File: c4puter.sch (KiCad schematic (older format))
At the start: 19 parts, among them J7 19V 3A, Q1 AOD4189, Q2 AOD4189, SW1 POWER, SW2 SW

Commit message: TODO: learn to write good commit messages
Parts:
- added C122: 100n, IPC7351-Nominal:CAPC1005X55, symbol C-0402
- added DS19: ACT, smd-semi:LED-0603, symbol LED-0603
- added DS20: POWER, smd-semi:LED-0603, symbol LED-0603
- added J9: PANEL, conn-100mil:CONN-100MIL-M-2x3, symbol CONN-100MIL-M-2x3
- added R14: 51, IPC7351-Nominal:RESC1005X40, symbol R-0402
- added R22, R52: 5k1, IPC7351-Nominal:RESC1005X40, symbol R-0402
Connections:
- net GND: now also C122.2, J9.1, J9.3, J9.5, R22.2, R52.2
- net at R71.2, R73.2, SW1.3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: now also J9.6
- net EC/BTN_PWR: now reaches C57.1, R73.1
- net EC/BTN_AUX: now reaches C59.1, R74.1
- new net: C122.1, R14.2
- new net: DS20.1 (K), R52.1
- new net: DS19.1 (K), R22.1
- new net CPU0/CCLK: R14.1
- new net EC/LED_ACT: DS19.2 (A), J9.4
- new net EC/LED_PWR: DS20.2 (A), J9.2
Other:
- note added: "Layout: route FPGA configuration data with\nstandard multidrop bus layout, rough length\nmatching between data and CCLK, fly-by\ntermination of CCLK."
- moved on the sheet: C57, C59, R73, R74

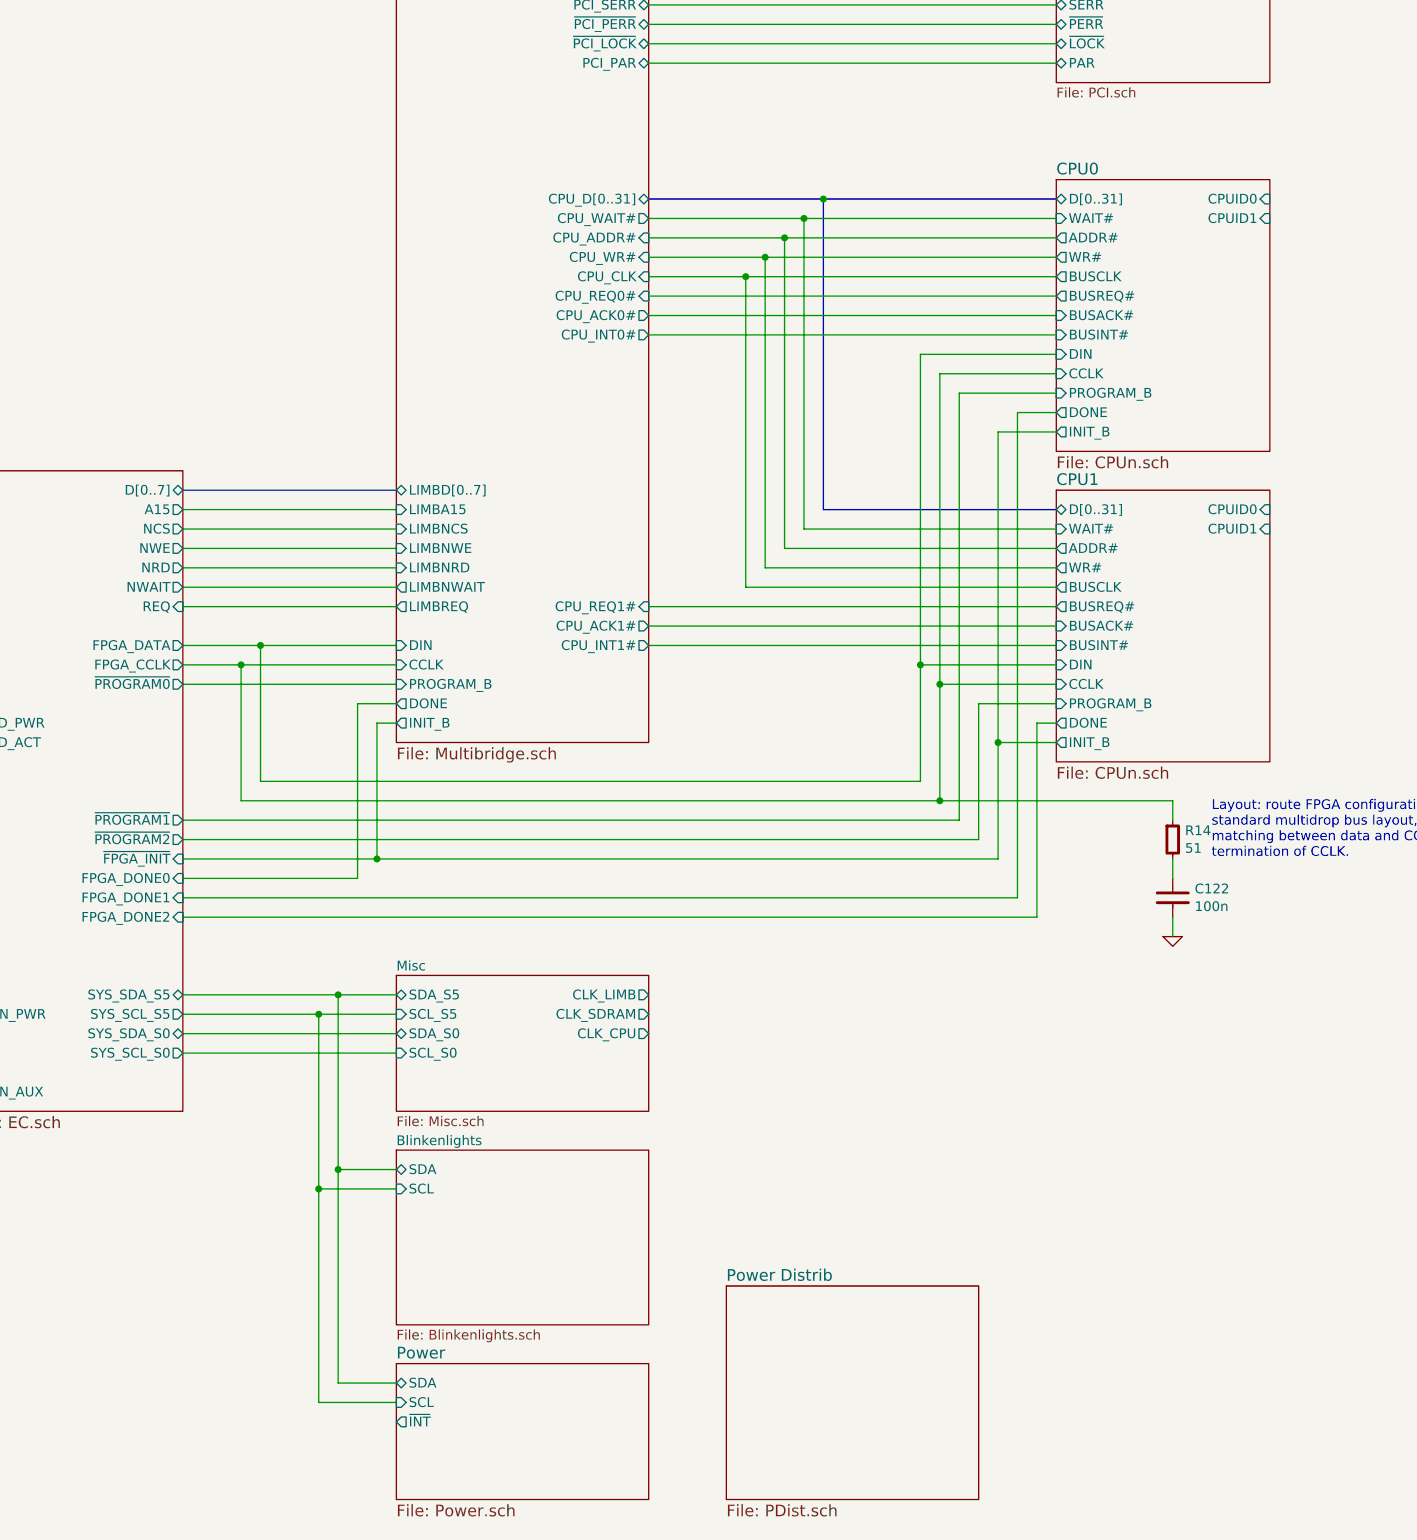
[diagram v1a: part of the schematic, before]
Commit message: Route clocks
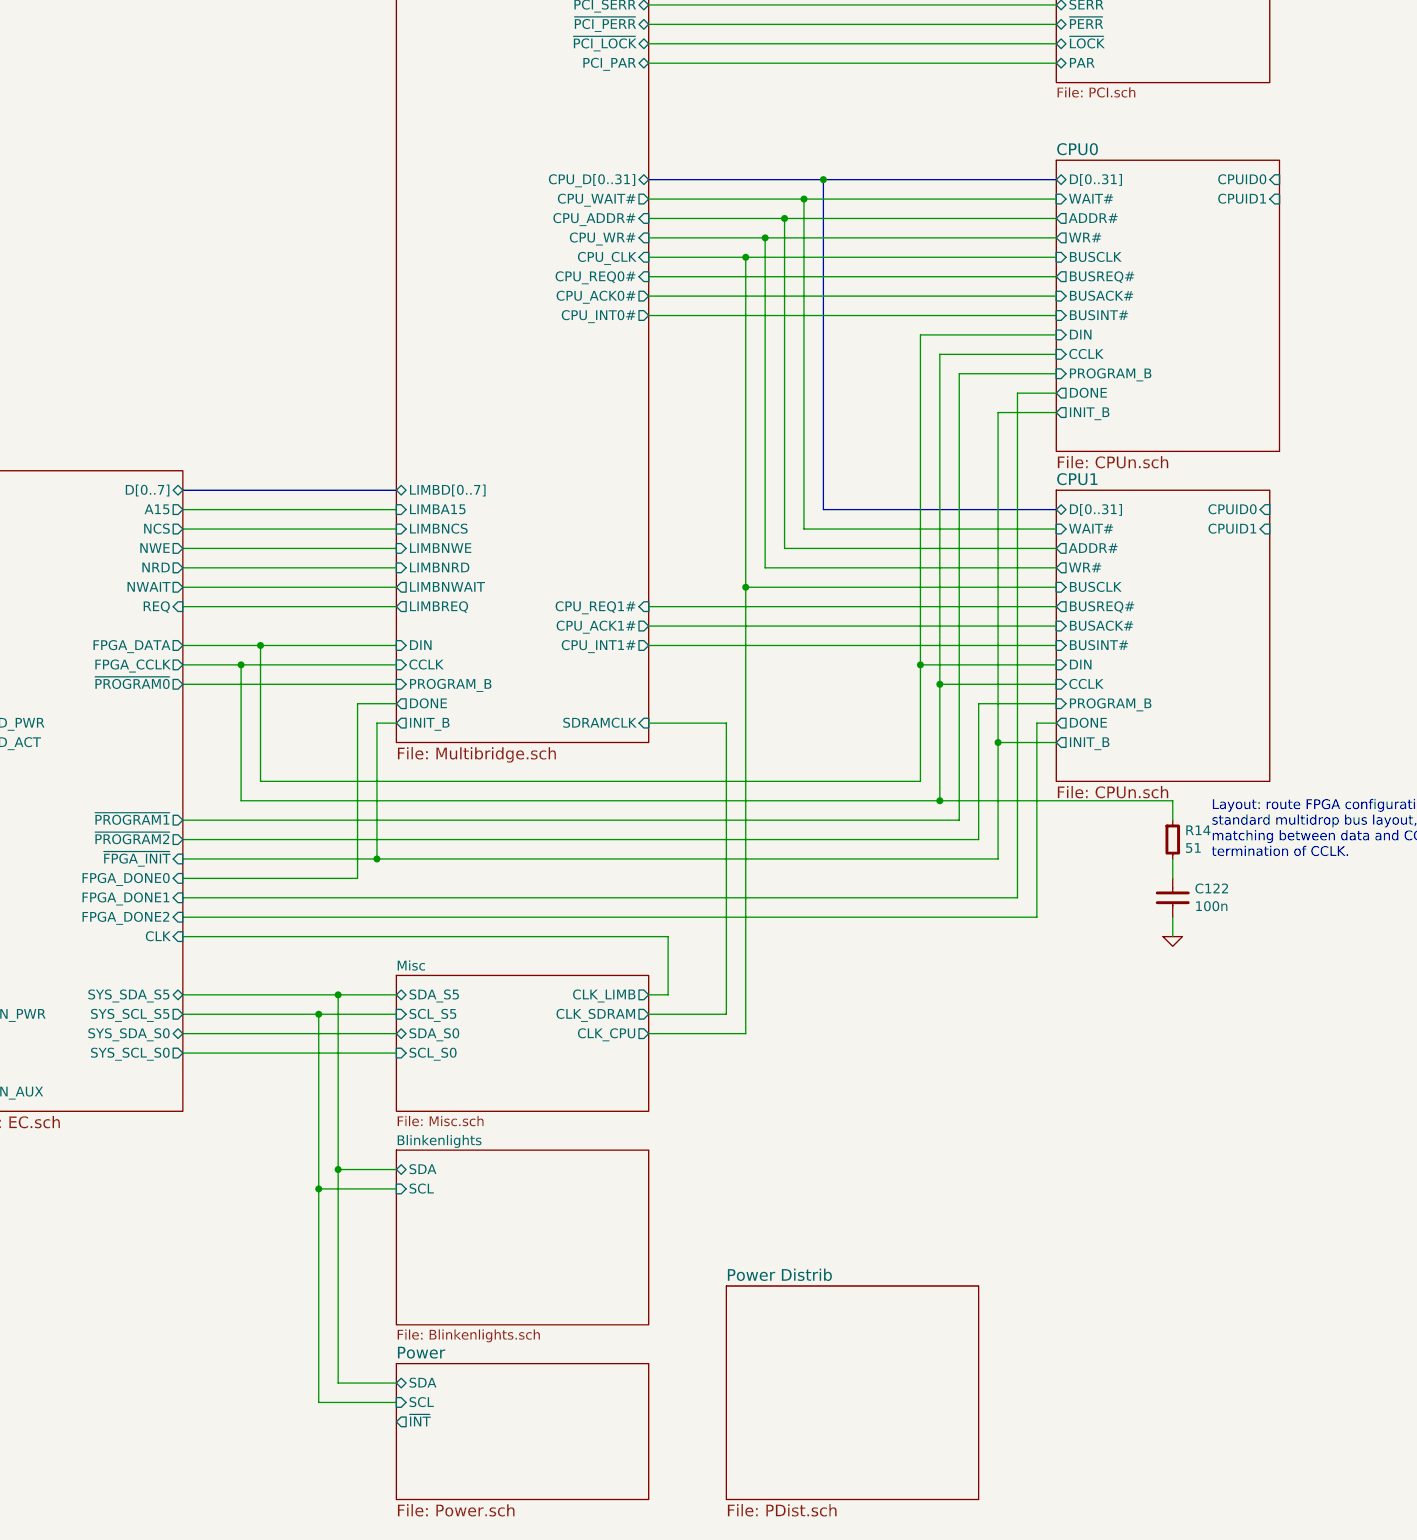
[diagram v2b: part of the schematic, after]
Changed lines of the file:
@@
 $EndSheet
 $Sheet
-S 10800 3200 1100 1400
+S 10800 3100 1150 1500
 U 5765A5BA
 F0 "CPU0" 60
 F1 "CPUn.sch" 60
-F2 "D[0..31]" B L 10800 3300 50
-F3 "WAIT#" I L 10800 3400 50
-F4 "ADDR#" O L 10800 3500 50
-F5 "WR#" O L 10800 3600 50
-F6 "BUSCLK" O L 10800 3700 50
-F7 "BUSREQ#" O L 10800 3800 50
-F8 "BUSACK#" I L 10800 3900 50
-F9 "BUSINT#" I L 10800 4000 50
-F10 "CPUID0" I R 11900 3300 50
-F11 "CPUID1" I R 11900 3400 50
-F12 "DIN" I L 10800 4100 50
-F13 "CCLK" I L 10800 4200 50
-F14 "PROGRAM_B" I L 10800 4300 50
-F15 "DONE" O L 10800 4400 50
-F16 "INIT_B" O L 10800 4500 50
-$EndSheet
-$Sheet
-S 10800 4800 1100 1400
-U 5765B2E6
-F0 "CPU1" 60
-F1 "CPUn.sch" 60
-F2 "D[0..31]" B L 10800 4900 50
-F3 "WAIT#" I L 10800 5000 50
-F4 "ADDR#" O L 10800 5100 50
-F5 "WR#" O L 10800 5200 50
-F6 "BUSCLK" O L 10800 5300 50
-F7 "BUSREQ#" O L 10800 5400 50
-F8 "BUSACK#" I L 10800 5500 50
-F9 "BUSINT#" I L 10800 5600 50
-F10 "CPUID0" I R 11900 4900 50
-F11 "CPUID1" I R 11900 5000 50
-F12 "DIN" I L 10800 5700 50
-F13 "CCLK" I L 10800 5800 50
-F14 "PROGRAM_B" I L 10800 5900 50
-F15 "DONE" O L 10800 6000 50
-F16 "INIT_B" O L 10800 6100 50
+F2 "D[0..31]" B L 10800 3200 50
+F3 "WAIT#" I L 10800 3300 50
+F4 "ADDR#" O L 10800 3400 50
+F5 "WR#" O L 10800 3500 50
+F6 "BUSREQ#" O L 10800 3700 50
+F7 "BUSACK#" I L 10800 3800 50
+F8 "BUSINT#" I L 10800 3900 50
+F9 "CPUID0" I R 11950 3200 50
+F10 "CPUID1" I R 11950 3300 50
+F11 "DIN" I L 10800 4000 50
+F12 "CCLK" I L 10800 4100 50
+F13 "PROGRAM_B" I L 10800 4200 50
+F14 "DONE" O L 10800 4300 50
+F15 "INIT_B" O L 10800 4400 50
+F16 "BUSCLK" I L 10800 3600 50
 $EndSheet
 $Sheet
@@
 F24 "SYS_SCL_S0" O R 6300 7700 50
 F25 "SYS_SDA_S0" B R 6300 7600 50
+F26 "CLK" I R 6300 7100 50
 $EndSheet
 $Comp
@@
 F12 "DONE" O L 7400 5900 50
 F13 "INIT_B" O L 7400 6000 50
-F14 "CPU_D[0..31]" B R 8700 3300 50
-F15 "CPU_WAIT#" O R 8700 3400 50
-F16 "CPU_ADDR#" I R 8700 3500 50
-F17 "CPU_WR#" I R 8700 3600 50
-F18 "CPU_CLK" I R 8700 3700 50
-F19 "CPU_REQ0#" I R 8700 3800 50
-F20 "CPU_ACK0#" O R 8700 3900 50
+F14 "CPU_D[0..31]" B R 8700 3200 50
+F15 "CPU_WAIT#" O R 8700 3300 50
+F16 "CPU_ADDR#" I R 8700 3400 50
+F17 "CPU_WR#" I R 8700 3500 50
+F18 "CPU_CLK" I R 8700 3600 50
+F19 "CPU_REQ0#" I R 8700 3700 50
+F20 "CPU_ACK0#" O R 8700 3800 50
 F21 "CPU_REQ1#" I R 8700 5400 50
 F22 "CPU_ACK1#" O R 8700 5500 50
-F23 "CPU_INT0#" O R 8700 4000 50
+F23 "CPU_INT0#" O R 8700 3900 50
 F24 "CPU_INT1#" O R 8700 5600 50
 F25 "PCI_AD[0..31]" B R 8700 1200 50
@@
 F38 "~PCI_LOCK" B R 8700 2500 50
 F39 "PCI_PAR" B R 8700 2600 50
+F40 "SDRAMCLK" I R 8700 6000 50
 $EndSheet
 $Comp
@@
 	6300 5300 7400 5300
 Wire Bus Line
+	8700 3200 10800 3200
+Wire Wire Line
 	8700 3300 10800 3300
 Wire Wire Line
@@
 	8700 3600 10800 3600
 Wire Wire Line
-	8700 3700 10800 3700
-Wire Wire Line
-	10800 3800 8700 3800
-Wire Wire Line
-	10800 3900 8700 3900
-Wire Wire Line
-	10800 4000 8700 4000
-Wire Wire Line
 	8700 5400 10800 5400
 Wire Wire Line
@@
 	10800 5300 9200 5300
 Wire Wire Line
-	9200 5300 9200 3700
-Connection ~ 9200 3700
+	9200 3600 9200 7600
+Connection ~ 9200 3600
 Wire Wire Line
 	10800 5200 9300 5200
 Wire Wire Line
-	9300 5200 9300 3600
-Connection ~ 9300 3600
+	9300 5200 9300 3500
+Connection ~ 9300 3500
 Wire Wire Line
 	10800 5100 9400 5100
 Wire Wire Line
-	9400 5100 9400 3500
-Connection ~ 9400 3500
+	9400 5100 9400 3400
+Connection ~ 9400 3400
 Wire Wire Line
 	10800 5000 9500 5000
 Wire Wire Line
-	9500 5000 9500 3400
-Connection ~ 9500 3400
+	9500 5000 9500 3300
+Connection ~ 9500 3300
 Wire Bus Line
 	10800 4900 9600 4900
 Wire Bus Line
-	9600 4900 9600 3300
-Connection ~ 9600 3300
+	9600 4900 9600 3200
+Connection ~ 9600 3200
 Wire Bus Line
 	8700 1200 10800 1200
@@
 	6700 6300 10100 6300
 Wire Wire Line
-	10100 6300 10100 4100
-Wire Wire Line
-	10100 4100 10800 4100
+	10100 6300 10100 4000
+Wire Wire Line
+	10100 4000 10800 4000
 Connection ~ 6700 5600
 Wire Wire Line
@@
 Connection ~ 10100 5700
 Wire Wire Line
-	10800 4200 10200 4200
-Wire Wire Line
-	10200 4200 10200 6400
+	10800 4100 10200 4100
+Wire Wire Line
+	10200 4100 10200 6400
 Wire Wire Line
 	6600 6400 11400 6400
@@
 	6300 6500 10300 6500
 Wire Wire Line
-	10300 6500 10300 4300
-Wire Wire Line
-	10300 4300 10800 4300
+	10300 6500 10300 4200
+Wire Wire Line
+	10300 4200 10800 4200
 Wire Wire Line
 	10800 5800 10200 5800
@@
 	7300 6000 7400 6000
 Wire Wire Line
-	10500 4500 10500 6700
-Wire Wire Line
-	10500 4500 10800 4500
+	10500 4400 10500 6700
+Wire Wire Line
+	10500 4400 10800 4400
 Connection ~ 7300 6700
 Wire Wire Line
@@
 	6300 6900 10600 6900
 Wire Wire Line
-	10600 6900 10600 4400
-Wire Wire Line
-	10600 4400 10800 4400
+	10600 6900 10600 4300
+Wire Wire Line
+	10600 4300 10800 4300
 Wire Wire Line
 	6300 7000 10700 7000
@@
 	7000 9500 7400 9500
 Wire Wire Line
-	7000 9500 7000 7500
+	7000 7500 7000 9500
 Connection ~ 7000 7500
 Wire Wire Line
@@
 	7400 8300 7100 8300
 Connection ~ 7100 8300
+Wire Wire Line
+	8700 3700 10800 3700
+Wire Wire Line
+	8700 3800 10800 3800
+Wire Wire Line
+	8700 3900 10800 3900
+$Sheet
+S 10800 4800 1100 1500
+U 5765B2E6
+F0 "CPU1" 60
+F1 "CPUn.sch" 60
+F2 "D[0..31]" B L 10800 4900 50
+F3 "WAIT#" I L 10800 5000 50
+F4 "ADDR#" O L 10800 5100 50
+F5 "WR#" O L 10800 5200 50
+F6 "BUSREQ#" O L 10800 5400 50
+F7 "BUSACK#" I L 10800 5500 50
+F8 "BUSINT#" I L 10800 5600 50
+F9 "CPUID0" I R 11900 4900 50
+F10 "CPUID1" I R 11900 5000 50
+F11 "DIN" I L 10800 5700 50
+F12 "CCLK" I L 10800 5800 50
+F13 "PROGRAM_B" I L 10800 5900 50
+F14 "DONE" O L 10800 6000 50
+F15 "INIT_B" O L 10800 6100 50
+F16 "BUSCLK" I L 10800 5300 50
+$EndSheet
+Wire Wire Line
+	9200 7600 8700 7600
+Connection ~ 9200 5300
+Wire Wire Line
+	8700 6000 9100 6000
+Wire Wire Line
+	9100 6000 9100 7500
+Wire Wire Line
+	9100 7500 8700 7500
+Wire Wire Line
+	6300 7100 8800 7100
+Wire Wire Line
+	8800 7100 8800 7400
+Wire Wire Line
+	8800 7400 8700 7400
 $EndSCHEMATC

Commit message: Add SDRAM SPD to I2C
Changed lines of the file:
@@
 F16 "BUSCLK" I L 10800 3600 50
-$EndSheet
-$Sheet
-S 5200 4700 1100 3300
-U 5765CB89
-F0 "EC" 60
-F1 "EC.sch" 60
-F2 "D[0..7]" B R 6300 4800 50
-F3 "A15" O R 6300 4900 50
-F4 "NCS" O R 6300 5000 50
-F5 "NWE" O R 6300 5100 50
-F6 "NRD" O R 6300 5200 50
-F7 "NWAIT" O R 6300 5300 50
-F8 "FPGA_DATA" O R 6300 5600 50
-F9 "FPGA_CCLK" O R 6300 5700 50
-F10 "~PROGRAM0" O R 6300 5800 50
-F11 "~PROGRAM2" O R 6300 6600 50
-F12 "~PROGRAM1" O R 6300 6500 50
-F13 "~FPGA_INIT" I R 6300 6700 50
-F14 "FPGA_DONE0" I R 6300 6800 50
-F15 "FPGA_DONE1" I R 6300 6900 50
-F16 "FPGA_DONE2" I R 6300 7000 50
-F17 "REQ" I R 6300 5400 50
-F18 "BTN_PWR" I L 5200 7500 50
-F19 "BTN_AUX" I L 5200 7900 50
-F20 "LED_PWR" O L 5200 6000 50
-F21 "LED_ACT" O L 5200 6100 50
-F22 "SYS_SCL_S5" O R 6300 7500 50
-F23 "SYS_SDA_S5" B R 6300 7400 50
-F24 "SYS_SCL_S0" O R 6300 7700 50
-F25 "SYS_SDA_S0" B R 6300 7600 50
-F26 "CLK" I R 6300 7100 50
 $EndSheet
 $Comp
@@
 F39 "PCI_PAR" B R 8700 2600 50
 F40 "SDRAMCLK" I R 8700 6000 50
+F41 "SDA" B L 7400 4500 50
+F42 "SCL" I L 7400 4600 50
 $EndSheet
 $Comp
@@
 Wire Wire Line
 	8800 7400 8700 7400
+$Sheet
+S 5200 4700 1100 3300
+U 5765CB89
+F0 "EC" 60
+F1 "EC.sch" 60
+F2 "D[0..7]" B R 6300 4800 50
+F3 "A15" O R 6300 4900 50
+F4 "NCS" O R 6300 5000 50
+F5 "NWE" O R 6300 5100 50
+F6 "NRD" O R 6300 5200 50
+F7 "NWAIT" O R 6300 5300 50
+F8 "FPGA_DATA" O R 6300 5600 50
+F9 "FPGA_CCLK" O R 6300 5700 50
+F10 "~PROGRAM0" O R 6300 5800 50
+F11 "~PROGRAM2" O R 6300 6600 50
+F12 "~PROGRAM1" O R 6300 6500 50
+F13 "~FPGA_INIT" I R 6300 6700 50
+F14 "FPGA_DONE0" I R 6300 6800 50
+F15 "FPGA_DONE1" I R 6300 6900 50
+F16 "FPGA_DONE2" I R 6300 7000 50
+F17 "REQ" I R 6300 5400 50
+F18 "BTN_PWR" I L 5200 7500 50
+F19 "BTN_AUX" I L 5200 7900 50
+F20 "LED_PWR" O L 5200 6000 50
+F21 "LED_ACT" O L 5200 6100 50
+F22 "SYS_SCL_S5" O R 6300 7500 50
+F23 "SYS_SDA_S5" B R 6300 7400 50
+F24 "SYS_SCL_S0" O R 6300 7700 50
+F25 "SYS_SDA_S0" B R 6300 7600 50
+F26 "CLK" I R 6300 7100 50
+$EndSheet
+Wire Wire Line
+	7400 4600 6900 4600
+Wire Wire Line
+	6900 4600 6900 7700
+Connection ~ 6900 7700
+Wire Wire Line
+	6800 7600 6800 4500
+Wire Wire Line
+	6800 4500 7400 4500
+Connection ~ 6800 7600
 $EndSCHEMATC

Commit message: Route PCI SMBUS
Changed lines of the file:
@@
 	6700 5600 6700 6300
 Wire Wire Line
-	6700 6300 10100 6300
-Wire Wire Line
-	10100 6300 10100 4000
+	10100 6300 6700 6300
+Wire Wire Line
+	10100 4000 10100 6300
 Wire Wire Line
 	10100 4000 10800 4000
@@
 F25 "SYS_SDA_S0" B R 6300 7600 50
 F26 "CLK" I R 6300 7100 50
+F27 "PCI_SDA" B L 5200 4800 50
+F28 "PCI_SCL" B L 5200 4900 50
 $EndSheet
 Wire Wire Line
@@
 	6800 4500 7400 4500
 Connection ~ 6800 7600
+Wire Wire Line
+	5200 4800 5000 4800
+Wire Wire Line
+	5000 4800 5000 900
+Wire Wire Line
+	5000 900  12300 900
+Wire Wire Line
+	12300 900  12300 1700
+Wire Wire Line
+	12300 1700 11900 1700
+Wire Wire Line
+	5200 4900 4900 4900
+Wire Wire Line
+	4900 4900 4900 800
+Wire Wire Line
+	4900 800  12400 800
+Wire Wire Line
+	12400 800  12400 1600
+Wire Wire Line
+	12400 1600 11900 1600
 $EndSCHEMATC
